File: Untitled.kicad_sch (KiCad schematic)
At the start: 4 parts, among them J3 Conn_01x02, U7 MAX98357AEWL+T

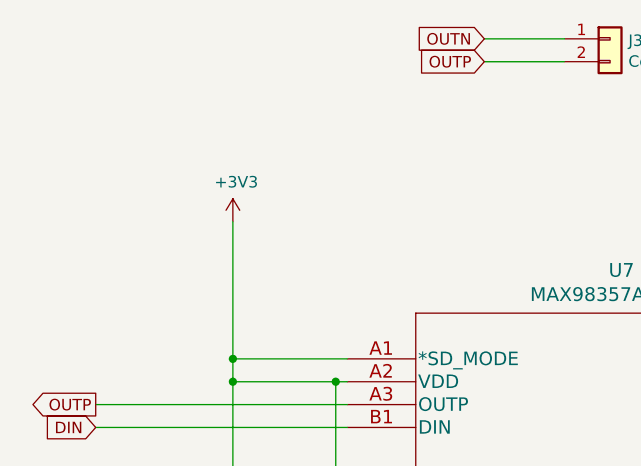
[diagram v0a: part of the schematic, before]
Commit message: reverting to KiCad 7
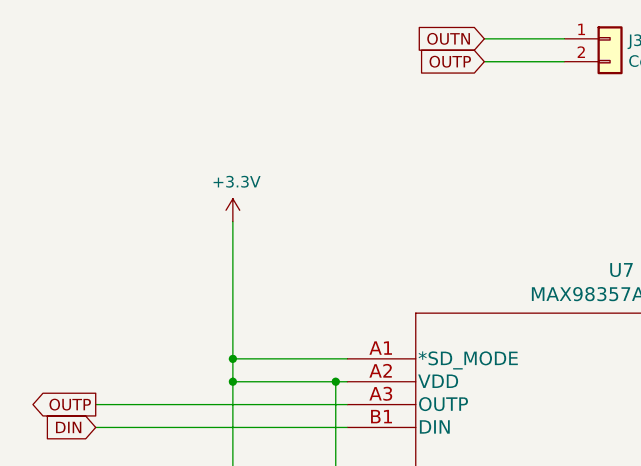
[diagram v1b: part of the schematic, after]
